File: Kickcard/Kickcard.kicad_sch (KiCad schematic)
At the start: 23 parts, among them J1 Conn_Side_Expansion, J2 Conn_01x01_Pin, SW1 SW_DIP_x04, SW2 SW_MEC_5E, SW3 SW_MEC_5E, U1 PAL20L8, U2 SST39SF040, U3 SST39SF040, U4 27C400

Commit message: added test points
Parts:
- removed J2: Conn_01x01_Pin, Connector_PinHeader_2.54mm:PinHeader_1x01_P2.54mm_Vertical, symbol Connector:Conn_01x01_Pin
- added 7Mhz1, A1, A10, A11, A12, A13, A14, A15, A16, A17, A18, A19, A2, A20, A21, A22, A23, A3, A4, A5, A6, A7, A8, A9, AS1, CCK1, CCKQ1, Clk_in1, D0, D1, D10, D11, D12, D13, D14, D15, D2, D3, D4, D5, D6, D7, D8, D9, DTACK1, LDS1, R/W1, UDS1: Conn_01x01, TestPoint:TestPoint_Pad_D1.0mm, symbol Connector_Generic:Conn_01x01
- renumbered D1 to DI1, D2 to DI2, D3 to DI3
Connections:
- net 7MHz: now also 7Mhz1.1 (Pin_1)
- net A1: now also A1.1 (Pin_1)
- net A10: now also A10.1 (Pin_1)
- net A11: now also A11.1 (Pin_1)
- net A12: now also A12.1 (Pin_1)
- net A13: now also A13.1 (Pin_1)
- net A14: now also A14.1 (Pin_1)
- net A15: now also A15.1 (Pin_1)
- net A16: now also A16.1 (Pin_1)
- net A17: now also A17.1 (Pin_1)
- net A18: now also A18.1 (Pin_1)
- net A19: now also A19.1 (Pin_1)
- net A2: now also A2.1 (Pin_1)
- net A20: now also A20.1 (Pin_1)
- net A21: now also A21.1 (Pin_1)
- net A22: now also A22.1 (Pin_1)
- net A23: now also A23.1 (Pin_1)
- net A3: now also A3.1 (Pin_1)
- net A4: now also A4.1 (Pin_1)
- net A5: now also A5.1 (Pin_1)
- net A6: now also A6.1 (Pin_1)
- net A7: now also A7.1 (Pin_1)
- net A8: now also A8.1 (Pin_1)
- net A9: now also A9.1 (Pin_1)
- net AS: now also AS1.1 (Pin_1)
- net CCK: now also CCK1.1 (Pin_1)
- net CCKQ: now also CCKQ1.1 (Pin_1)
- net CLK_IN: now also Clk_in1.1 (Pin_1)
- net D0: now also D0.1 (Pin_1)
- net D1: now also D1.1 (Pin_1)
- net D10: now also D10.1 (Pin_1)
- net D11: now also D11.1 (Pin_1)
- net D12: now also D12.1 (Pin_1)
- net D13: now also D13.1 (Pin_1)
- net D14: now also D14.1 (Pin_1)
- net D15: now also D15.1 (Pin_1)
- net D2: now also D2.1 (Pin_1)
- net D3: now also D3.1 (Pin_1)
- net D4: now also D4.1 (Pin_1)
- net D5: now also D5.1 (Pin_1)
- net D6: now also D6.1 (Pin_1)
- net D7: now also D7.1 (Pin_1)
- net D8: now also D8.1 (Pin_1)
- net D9: now also D9.1 (Pin_1)
- net DTACK: now also DTACK1.1 (Pin_1)
- net R/W: now also R/W1.1 (Pin_1)
- net LDS: now reaches J1.70 (_LDS)
- net LDS: now also LDS1.1 (Pin_1)
- net UDS: now reaches J1.72 (_UDS)
- net UDS: now also UDS1.1 (Pin_1)
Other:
- moved on the sheet: JP1, MES1, MES2, MES3, U1

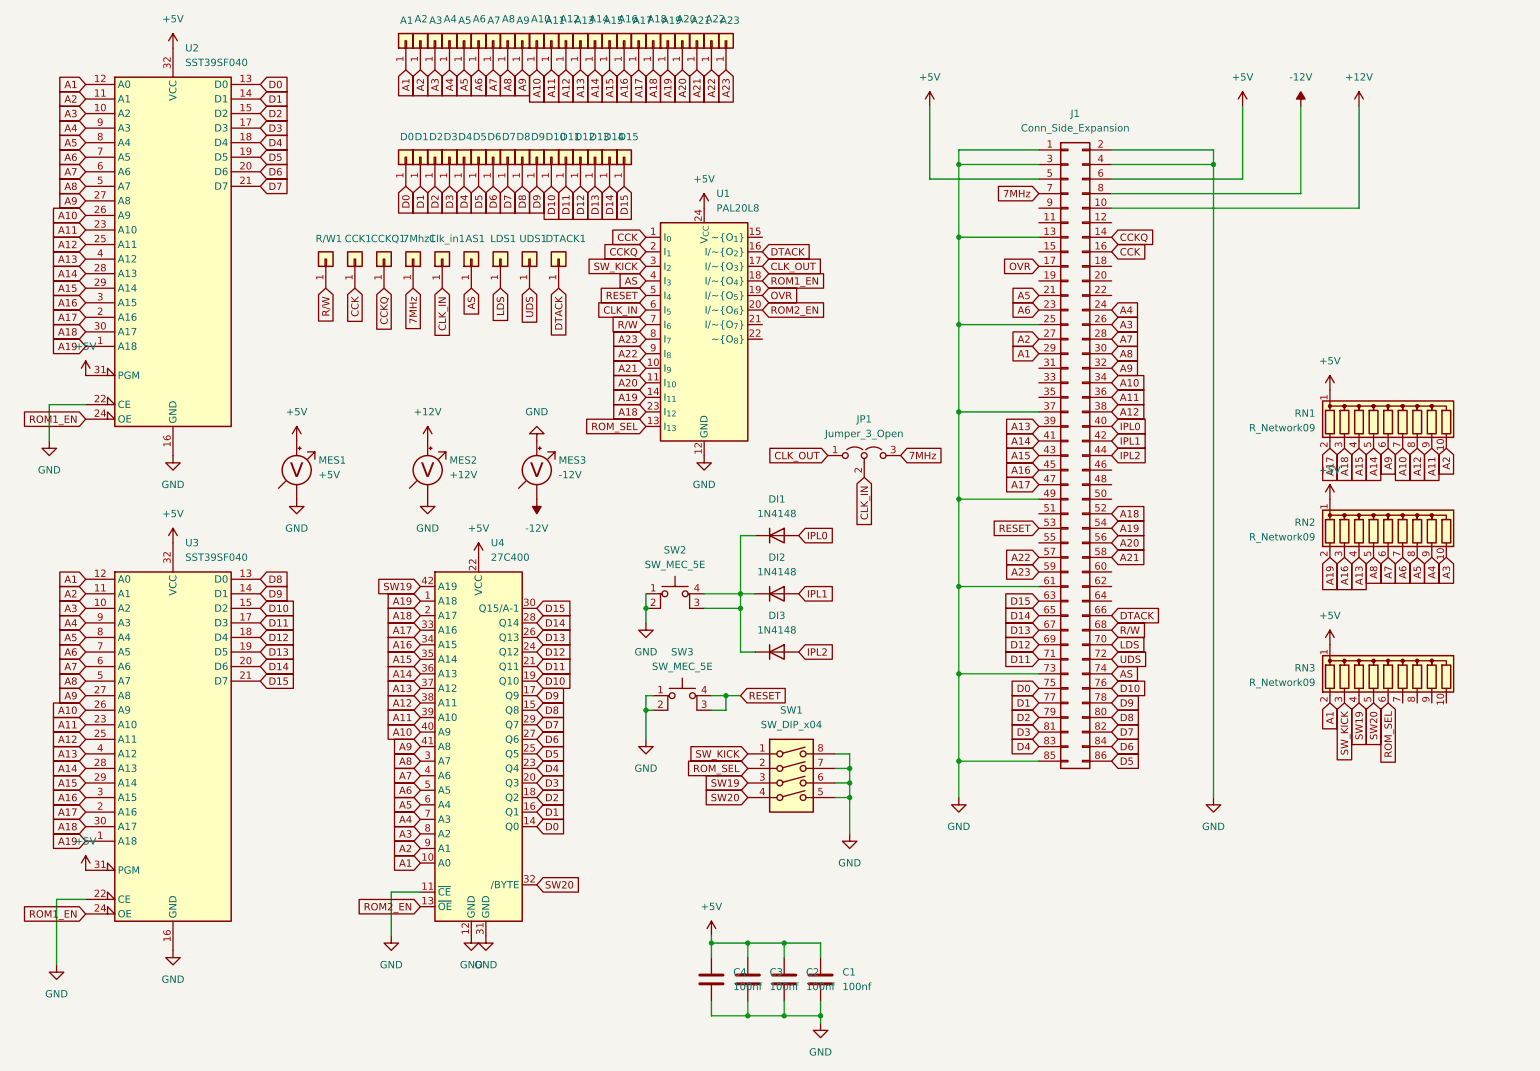
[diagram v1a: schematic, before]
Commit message: Big Design change
Remove test pins, extra rom and added "expansion" headers, corrected voltmeter footprint dimmensions
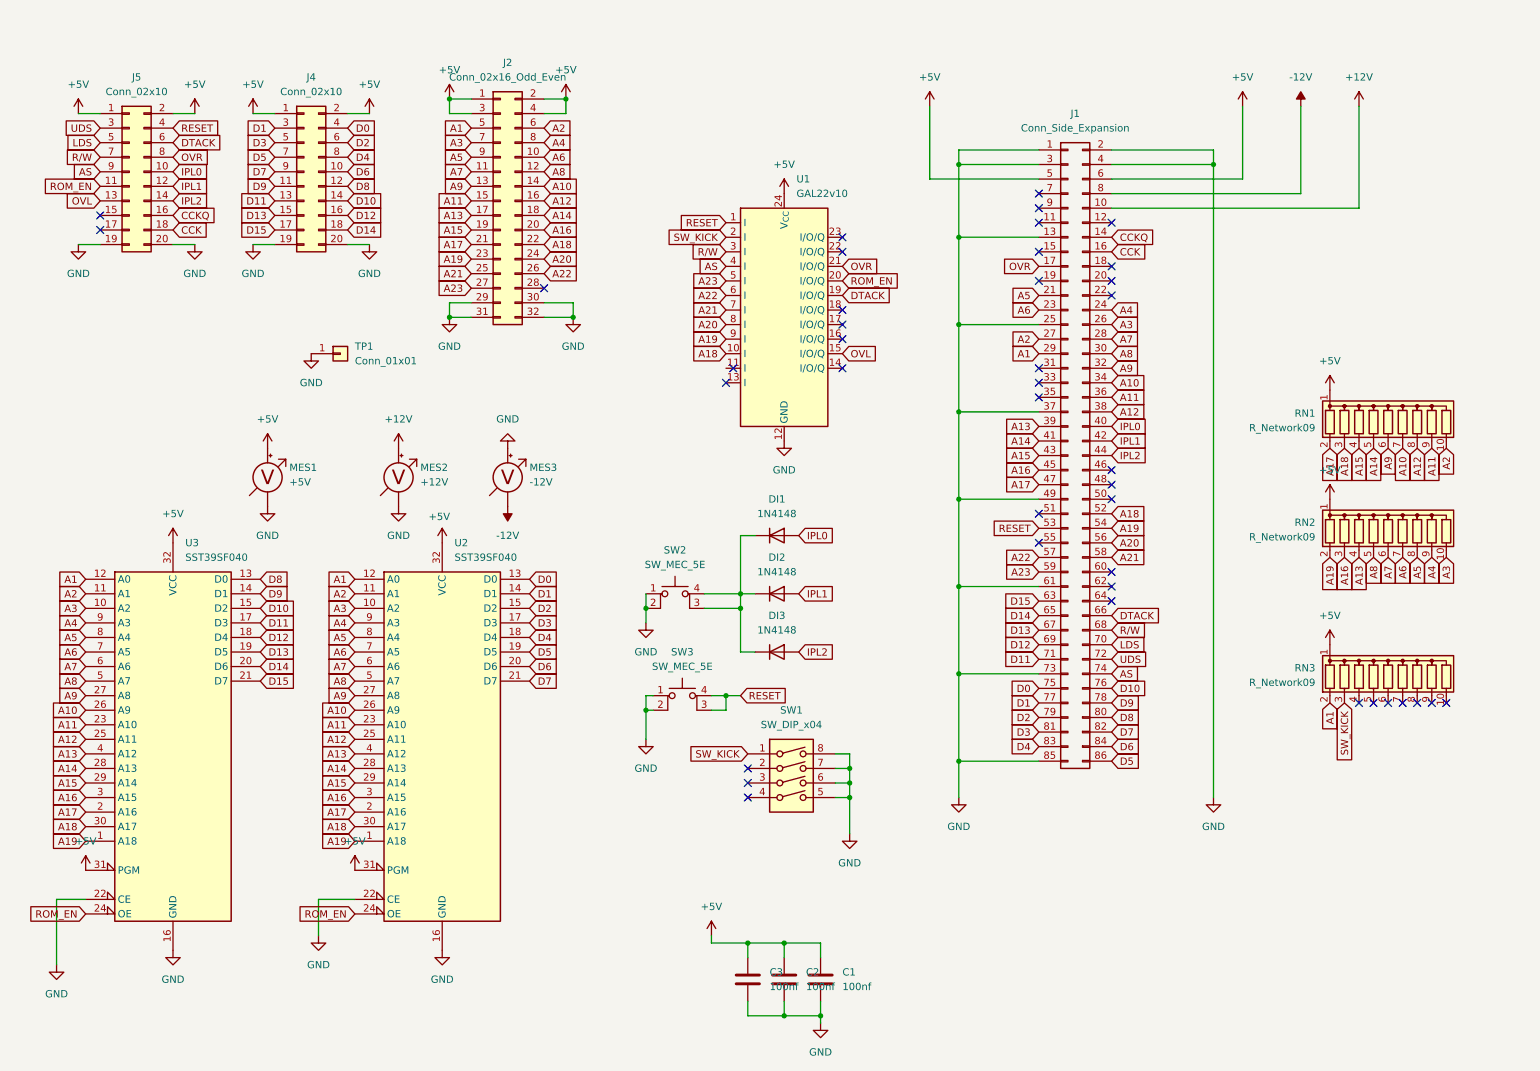
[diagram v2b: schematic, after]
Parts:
- removed 7Mhz1, A1, A10, A11, A12, A13, A14, A15, A16, A17, A18, A19, A2, A20, A21, A22, A23, A3, A4, A5, A6, A7, A8, A9, AS1, CCK1, CCKQ1, Clk_in1, D0, D1, D10, D11, D12, D13, D14, D15, D2, D3, D4, D5, D6, D7, D8, D9, DTACK1, LDS1, R/W1, UDS1: Conn_01x01, TestPoint:TestPoint_Pad_D1.0mm, symbol Connector_Generic:Conn_01x01
- removed C4: 100nf, Capacitor_THT:C_Disc_D3.0mm_W1.6mm_P2.50mm, symbol Device:C
- removed JP1: Jumper_3_Open, Connector_PinHeader_2.54mm:PinHeader_1x03_P2.54mm_Vertical, symbol Jumper:Jumper_3_Open
- removed U1: PAL20L8, Package_DIP:DIP-24_W7.62mm, symbol Logic_Programmable:PAL20L8
- removed U4: 27C400, Package_DIP:DIP-42_W15.24mm, symbol Amiga:27C400
- added J2: Conn_02x16_Odd_Even, Connector_PinHeader_2.54mm:PinHeader_2x16_P2.54mm_Vertical, symbol Connector_Generic:Conn_02x16_Odd_Even
- added J4, J5: Conn_02x10, Connector_PinHeader_2.54mm:PinHeader_2x10_P2.54mm_Vertical, symbol Connector_Generic:Conn_02x10_Odd_Even
- added TP1: Conn_01x01, TestPoint:TestPoint_Bridge_Pitch2.54mm_Drill1.0mm, symbol Connector_Generic:Conn_01x01
- added U1: GAL22v10, Package_DIP:DIP-24_W7.62mm, symbol Private:GAL22v10
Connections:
- net +5V: now also J2.1 (Pin_1), J2.2 (Pin_2), J2.3 (Pin_3), J2.4 (Pin_4), J4.1 (Pin_1), J4.2 (Pin_2), J5.1 (Pin_1), J5.2 (Pin_2), U1.24 (V_{CC})
- net A1: now also J2.5 (Pin_5)
- net A10: now also J2.14 (Pin_14)
- net A11: now also J2.15 (Pin_15)
- net A12: now also J2.16 (Pin_16)
- net A13: now also J2.17 (Pin_17)
- net A14: now also J2.18 (Pin_18)
- net A15: now also J2.19 (Pin_19)
- net A16: now also J2.20 (Pin_20)
- net A17: now also J2.21 (Pin_21)
- net A18: now also J2.22 (Pin_22), U1.10 (I)
- net A19: now also J2.23 (Pin_23), U1.9 (I)
- net A2: now also J2.6 (Pin_6)
- net A20: now also J2.24 (Pin_24), U1.8 (I)
- net A21: now also J2.25 (Pin_25), U1.7 (I)
- net A22: now also J2.26 (Pin_26), U1.6 (I)
- net A23: now also J2.27 (Pin_27), U1.5 (I)
- net A3: now also J2.7 (Pin_7)
- net A4: now also J2.8 (Pin_8)
- net A5: now also J2.9 (Pin_9)
- net A6: now also J2.10 (Pin_10)
- net A7: now also J2.11 (Pin_11)
- net A8: now also J2.12 (Pin_12)
- net A9: now also J2.13 (Pin_13)
- net AS: now also J5.9 (Pin_9), U1.4 (I)
- net CCK: now also J5.18 (Pin_18)
- net CCKQ: now also J5.16 (Pin_16)
- net D0: now also J4.4 (Pin_4)
- net D1: now also J4.3 (Pin_3)
- net D10: now also J4.14 (Pin_14)
- net D11: now also J4.13 (Pin_13)
- net D12: now also J4.16 (Pin_16)
- net D13: now also J4.15 (Pin_15)
- net D14: now also J4.18 (Pin_18)
- net D15: now also J4.17 (Pin_17)
- net D2: now also J4.6 (Pin_6)
- net D3: now also J4.5 (Pin_5)
- net D4: now also J4.8 (Pin_8)
- net D5: now also J4.7 (Pin_7)
- net D6: now also J4.10 (Pin_10)
- net D7: now also J4.9 (Pin_9)
- net D8: now also J4.12 (Pin_12)
- net D9: now also J4.11 (Pin_11)
- net DTACK: now also J5.6 (Pin_6), U1.19 (I/O/Q)
- net GND: now also J2.29 (Pin_29), J2.30 (Pin_30), J2.31 (Pin_31), J2.32 (Pin_32), J4.19 (Pin_19), J4.20 (Pin_20), J5.19 (Pin_19), J5.20 (Pin_20), TP1.1 (Pin_1), U1.12 (GND)
- net IPL0: now also J5.10 (Pin_10)
- net IPL1: now also J5.12 (Pin_12)
- net IPL2: now also J5.14 (Pin_14)
- net LDS: now also J5.5 (Pin_5)
- net OVR: now also J5.8 (Pin_8), U1.21 (I/O/Q)
- net RESET: now also J5.4 (Pin_4), U1.1 (I)
- net R/W: now also J5.7 (Pin_7), U1.3 (I)
- net SW_KICK: now also U1.2 (I)
- net UDS: now also J5.3 (Pin_3)
- net 7MHz: no longer names the net of J1.7 (7MHz_or_NC)
- net ROM1_EN renamed ROM_EN
- net ROM_EN: now also J5.11 (Pin_11), U1.20 (I/O/Q)
- net ROM_SEL: no longer names the net of SW1.2
- net ROM_SEL: no longer RN3.6 (R5)
- net SW19: no longer names the net of SW1.3
- net SW19: no longer RN3.4 (R3)
- net SW20: no longer names the net of SW1.4
- net SW20: no longer RN3.5 (R4)
- new net OVL: J5.13 (Pin_13), U1.15 (I/O/Q)
- no-connect marks 0 -> 41
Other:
- moved on the sheet: MES1, MES2, MES3, U2

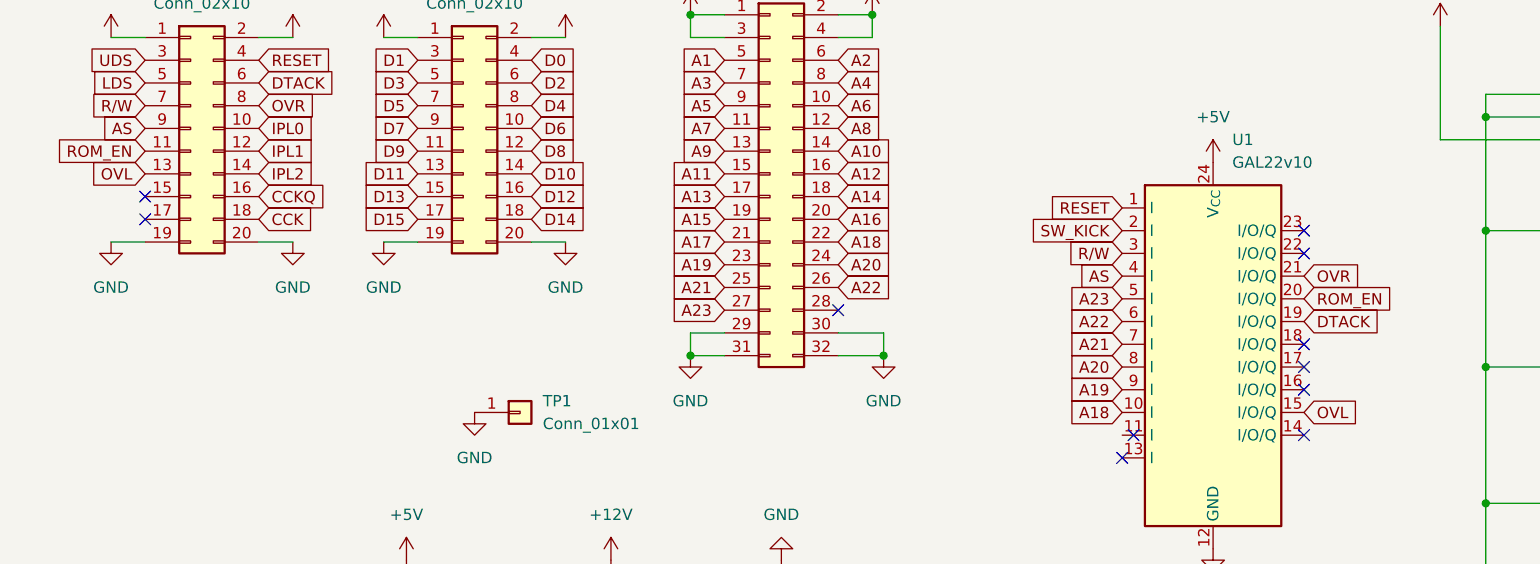
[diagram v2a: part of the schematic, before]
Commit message: small update
Added EXP1 and EXP2 ins from GAL to expansion header
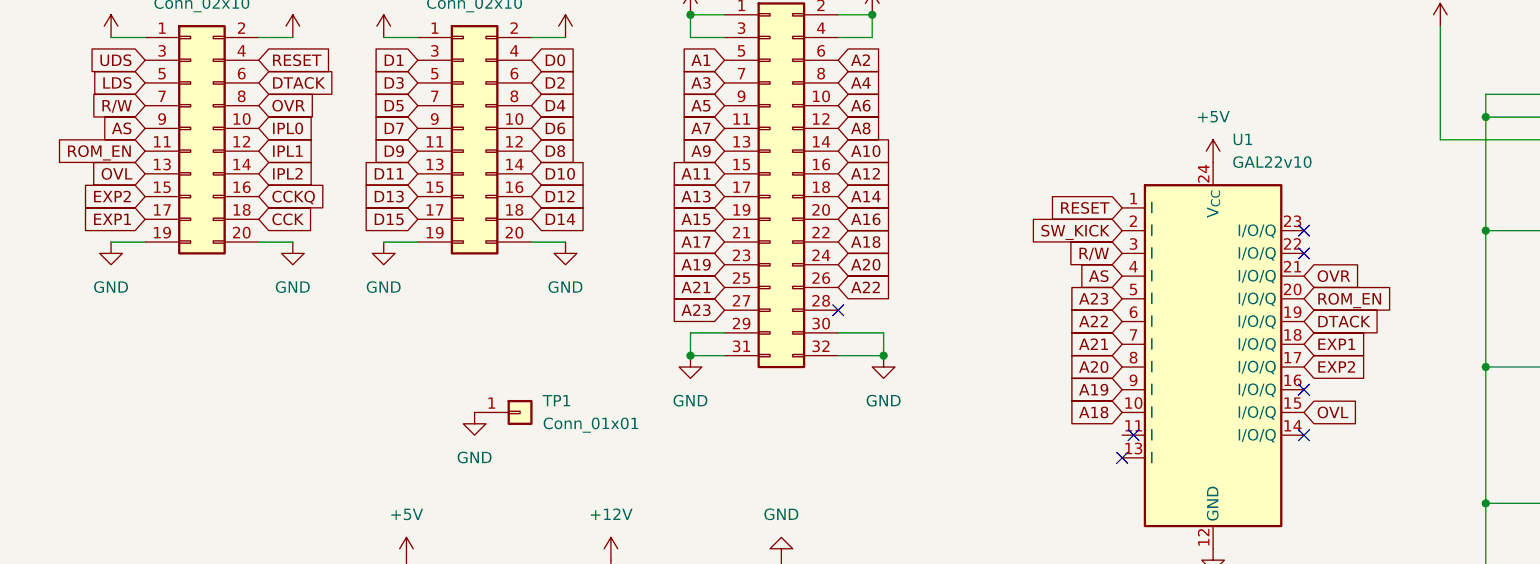
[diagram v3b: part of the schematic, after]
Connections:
- net EXP2: now reaches U1.17 (I/O/Q)
- net EXP2: now also J5.15 (Pin_15)
- net EXP1: now reaches U1.18 (I/O/Q)
- net EXP1: now also J5.17 (Pin_17)
- no-connect marks 41 -> 37
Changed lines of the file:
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@@
 	)
 	(no_connect
-		(at 160.02 68.58)
-	)
-	(no_connect
 		(at 143.51 151.13)
 	)
@@
 	)
 	(no_connect
-		(at 160.02 66.04)
-	)
-	(no_connect
 		(at 252.73 134.62)
 	)
@@
 	)
 	(no_connect
-		(at 30.48 49.53)
-	)
-	(no_connect
 		(at 107.95 62.23)
 	)
@@
 	)
 	(no_connect
-		(at 30.48 52.07)
-	)
-	(no_connect
 		(at 207.01 93.98)
 	)
@@
 		)
 	)
+	(global_label "EXP1"
+		(shape input)
+		(at 160.02 66.04 0)
+		(fields_autoplaced yes)
+		(effects
+			(font
+				(size 1.27 1.27)
+			)
+			(justify left)
+		)
+		(property "Intersheetrefs" "${INTERSHEET_REFS}"
+			(at 167.8432 66.04 0)
+			(effects
+				(font
+					(size 1.27 1.27)
+				)
+				(justify left)
+				(hide yes)
+			)
+		)
+	)
 	(global_label "R{slash}W"
 		(shape input)
@@
 		)
 	)
+	(global_label "EXP2"
+		(shape input)
+		(at 160.02 68.58 0)
+		(fields_autoplaced yes)
+		(effects
+			(font
+				(size 1.27 1.27)
+			)
+			(justify left)
+		)
+		(property "Intersheetrefs" "${INTERSHEET_REFS}"
+			(at 167.8432 68.58 0)
+			(effects
+				(font
+					(size 1.27 1.27)
+				)
+				(justify left)
+				(hide yes)
+			)
+		)
+	)
 	(global_label "A11"
 		(shape input)
@@
 		)
 	)
+	(global_label "EXP2"
+		(shape input)
+		(at 30.48 49.53 180)
+		(fields_autoplaced yes)
+		(effects
+			(font
+				(size 1.27 1.27)
+			)
+			(justify right)
+		)
+		(property "Intersheetrefs" "${INTERSHEET_REFS}"
+			(at 22.6568 49.53 0)
+			(effects
+				(font
+					(size 1.27 1.27)
+				)
+				(justify right)
+				(hide yes)
+			)
+		)
+	)
 	(global_label "A18"
 		(shape input)
@@
 				(hide yes)
 			)
+		)
+	)
+	(global_label "EXP1"
+		(shape input)
+		(at 30.48 52.07 180)
+		(fields_autoplaced yes)
+		(effects
+			(font
+				(size 1.27 1.27)
+			)
+			(justify right)
+		)
+		(property "Intersheetrefs" "${INTERSHEET_REFS}"
+			(at 22.6568 52.07 0)
+			(effects
+				(font
+					(size 1.27 1.27)
+				)
+				(justify right)
+				(hide yes)
+			)

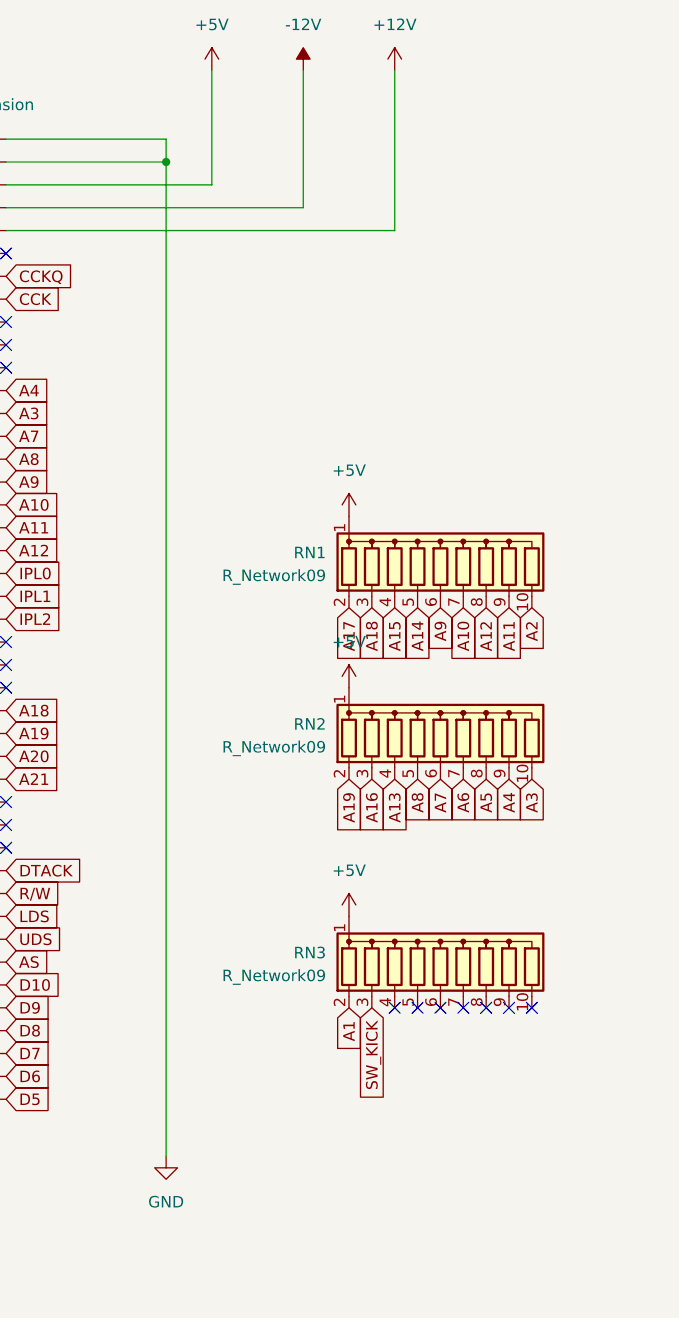
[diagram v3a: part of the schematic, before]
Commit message: added fixing holes
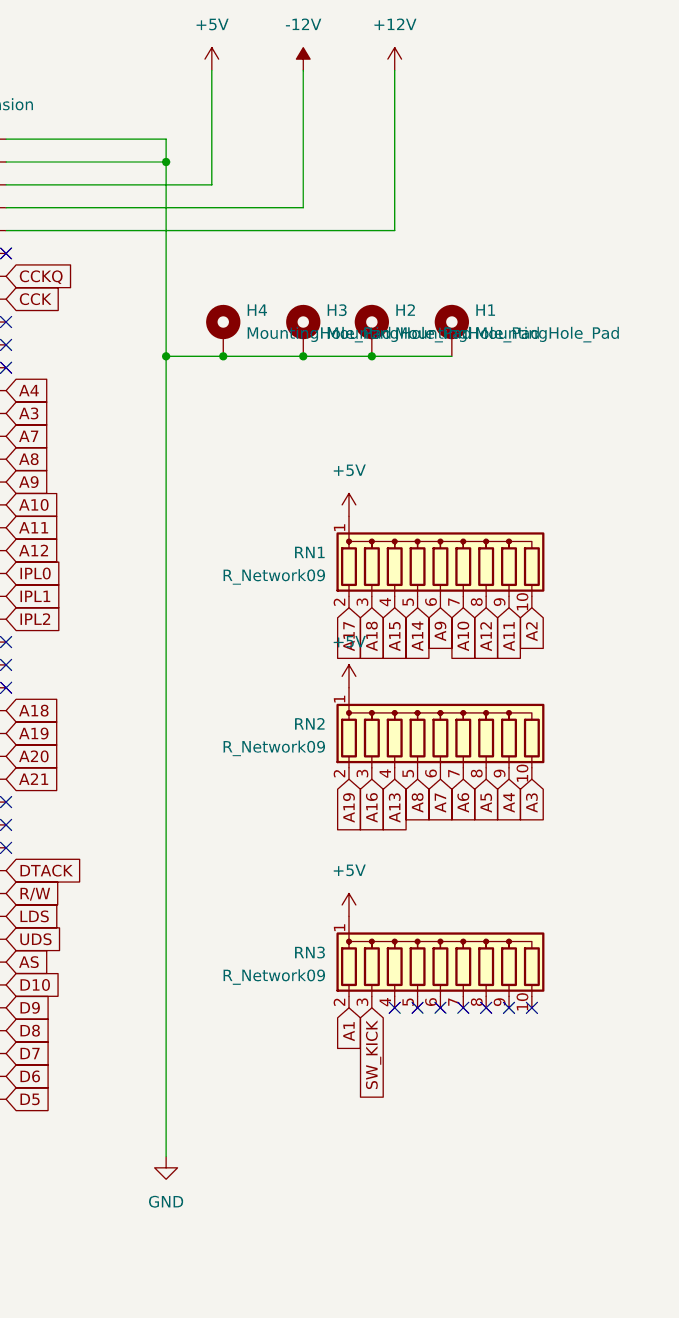
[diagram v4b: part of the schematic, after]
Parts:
- added H1, H2, H3, H4: MountingHole_Pad, MountingHole:MountingHole_3.2mm_M3_Pad_Via, symbol Mechanical:MountingHole_Pad
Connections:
- net GND: now also H1.1, H2.1, H3.1, H4.1
